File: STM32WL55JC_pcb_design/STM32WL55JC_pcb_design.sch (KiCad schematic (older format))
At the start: 32 parts, among them J1 Conn_01x03, J10 Conn_01x06_Male, J11 Conn_02x02_Odd_Even, J2 Conn_01x03, J3 Conn_02x05_Odd_Even, J4 Conn_01x03, J5 Conn_01x09, J6 Conn_01x09, J7 Conn_01x03, J8 Conn_01x09, J9 Conn_01x09, SW2 SW_MEC_5E, U1 STM32WL55JCI7, Y1 32MHz, Y2 32.768kHz

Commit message: Finish new design schematic
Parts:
- removed C13: 470nF, Capacitor_SMD:C_0805_2012Metric, symbol Device:C
- removed J10: Conn_01x06_Male, Connector_PinHeader_2.54mm:PinHeader_1x06_P2.54mm_Vertical, symbol Connector:Conn_01x06_Male
- removed J3: Conn_02x05_Odd_Even, Connector_PinHeader_1.27mm:PinHeader_2x05_P1.27mm_Vertical_SMD, symbol Connector_Generic:Conn_02x05_Odd_Even
- removed L1: 15uH, Inductor_SMD:L_0805_2012Metric, symbol pspice:INDUCTOR
- removed U1: STM32WL55JCI7, MCU_ST_STM3255JCI7:STM32WL55JCI7, symbol STM32WL55JC_pcb_design-rescue:STM32WL55JCI7-MCU_ST_STM3255JCI7
- added C11: 4.7F, Capacitor_SMD:C_0805_2012Metric, symbol Device:C
- added IC1: STM32F051R8T6, QFP50P1200X1200X160-64N, symbol STM32F051R8T6:STM32F051R8T6
- added J10: Conn_02x15_Odd_Even, symbol Connector_Generic:Conn_02x15_Odd_Even
- added J9: Conn_02x10_Odd_Even, symbol Connector_Generic:Conn_02x10_Odd_Even
- C12: renamed from C46; value 2.2pF -> 13pF
- C15: renamed from C53; value 2.2pF -> 13pF
- C3: value 100nF -> 4.7uF
- C6: renamed from C8; value 100nF -> 4.7uF
- C7: renamed from C9; value 100nF -> 10nF
- C8: renamed from C10; value 100nF -> 1uF
- Y1: footprint Oscillator:Oscillator_SMD_SeikoEpson_SG210-4Pin_2.5x2.0mm -> NX2016SA32MEXS00ACS06465:NX2016SA32MEXS00ACS06465
- renumbered C12 to C10, C47 to C13, C49 to C14, C7 to C5, C11 to C9, J4 to J3, J5 to J4, J6 to J5, J7 to J6, J8 to J7, J9 to J8, R7 to R1, SW2 to SW1
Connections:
- net labels added: ACC_ADC1, ACC_ADC2, ACC_ADC3, ACC_INT1, ACC_INT2, ADC_DIN, ADC_DOUT, ADC_SCLK, BOOT0, GPS_1PPS, GPS_AADET_N, GPS_EX_ANT, GPS_RESET, GPS_TIMER, LoRa_DO0, LoRa_DO1, LoRa_DO2, LoRa_DO3, LoRa_DO4, LoRa_DO5, LoRa_MISO, LoRa_MOSI, LoRa_NRST, LoRa_NSS, LoRa_RXTX_CTRL, LoRa_SCK, PA11, PB3, PB4, PC0, PC13, PD2, RTC_SQW, VDD
- net labels removed: ADC_DIN1, ADC_DIN2, ADC_DOUT1, ADC_DOUT2, ADC_SCLK1, ADC_SCLK2, PC5, RFI_N, RFI_P, RFO_HP, RFO_LP, RF_CTRL, SWO, VBAT, VDD1, VDD2, VDD3, VDD4, VDDA, VDDPA, VDDRF, VDDRF_1V55, VDDSMPS, VREF+, VR_PA
- wire segments 233 -> 160
- no-connect marks 10 -> 5
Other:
- moved on the sheet: C10, C12, C13, C14, C15, C5, C6, C7, C8, C9, J1, J11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

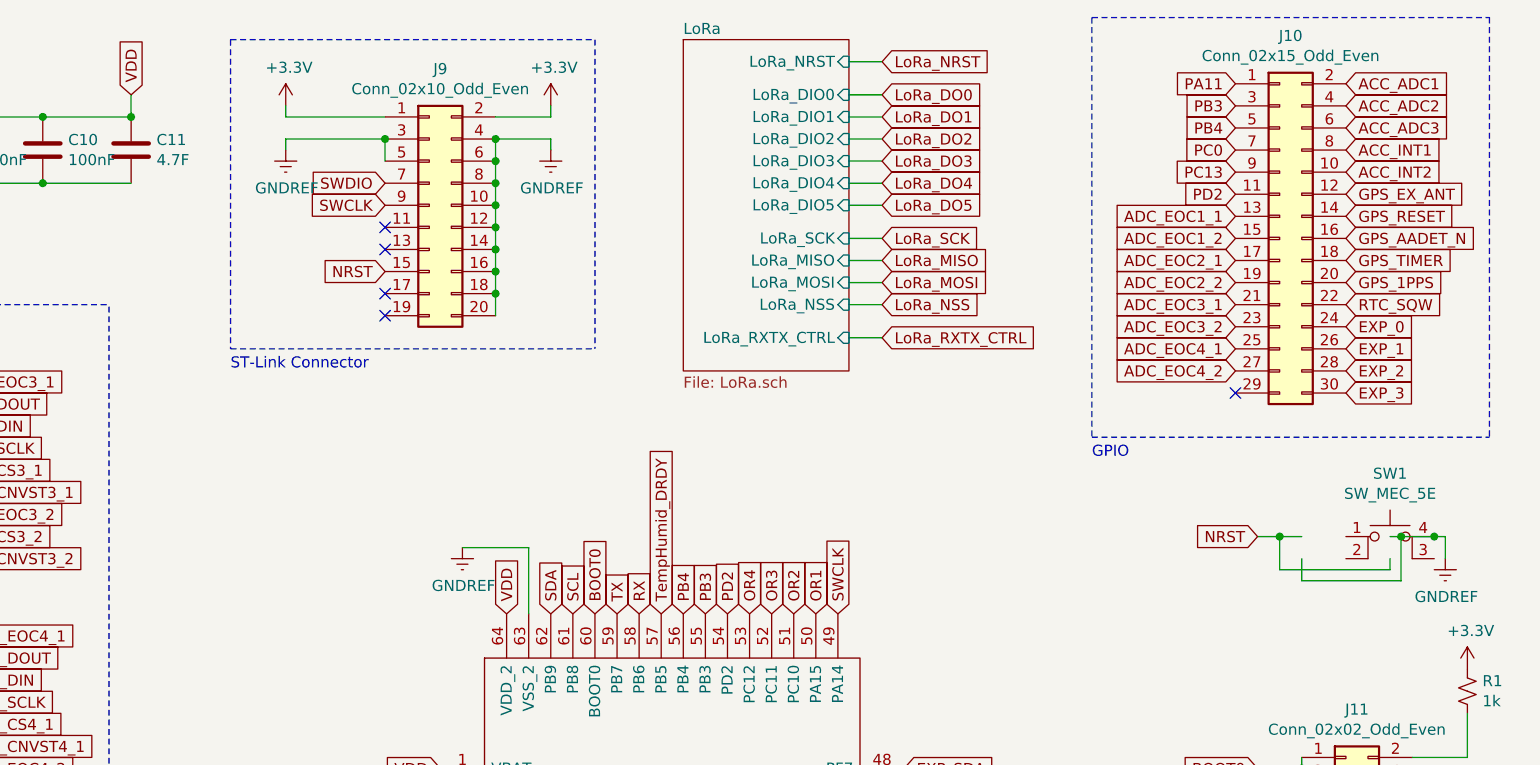
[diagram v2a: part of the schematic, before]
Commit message: Initial pcb layout and routing
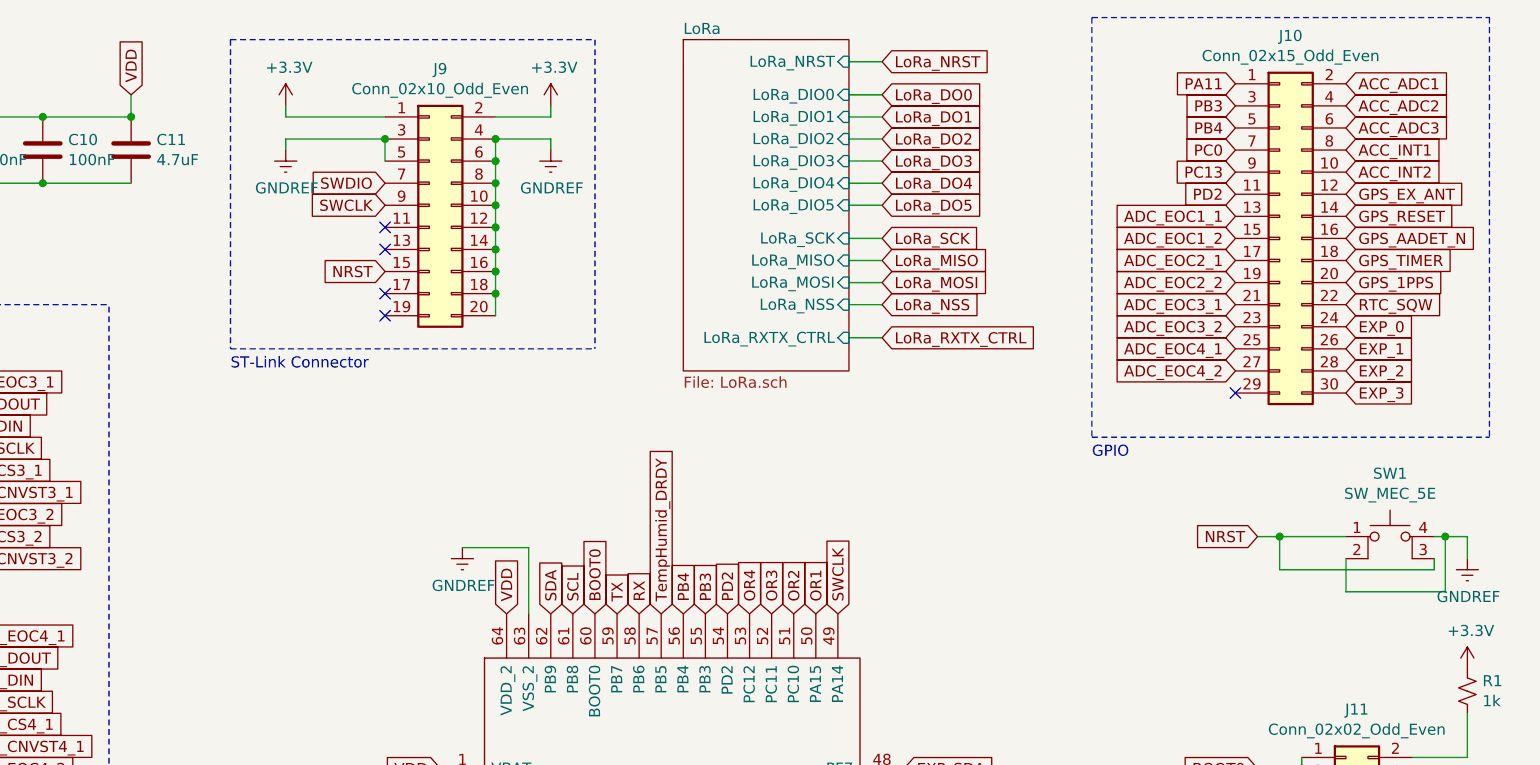
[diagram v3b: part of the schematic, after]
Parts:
- C11: value 4.7F -> 4.7uF
- C12, C15: footprint Capacitor_SMD:C_0805_2012Metric -> Capacitor_SMD:C_0402_1005Metric
- IC1: footprint QFP50P1200X1200X160-64N -> STM32F051R8T6:QFP50P1200X1200X160-64N
- J10: footprint (none) -> Connector_PinHeader_2.54mm:PinHeader_2x15_P2.54mm_Vertical
- J9: footprint (none) -> Connector_PinHeader_2.54mm:PinHeader_2x10_P2.54mm_Vertical
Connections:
- net GNDREF: now also SW1.2
- net NRST: now also SW1.1, SW1.3 (K)
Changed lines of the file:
@@
 F 0 "C12" H 9942 5246 50  0000 L CNN
 F 1 "13pF" H 9942 5155 50  0000 L CNN
-F 2 "Capacitor_SMD:C_0805_2012Metric" H 9850 5200 50  0001 C CNN
+F 2 "Capacitor_SMD:C_0402_1005Metric" H 9850 5200 50  0001 C CNN
 F 3 "~" H 9850 5200 50  0001 C CNN
 	1    9850 5200
@@
 F 0 "C15" H 10642 5246 50  0000 L CNN
 F 1 "13pF" H 10642 5155 50  0000 L CNN
-F 2 "Capacitor_SMD:C_0805_2012Metric" H 10550 5200 50  0001 C CNN
+F 2 "Capacitor_SMD:C_0402_1005Metric" H 10550 5200 50  0001 C CNN
 F 3 "~" H 10550 5200 50  0001 C CNN
 	1    10550 5200
@@
 $EndComp
 Wire Wire Line
-	10550 2900 10600 2900
-Wire Wire Line
-	10050 2900 10150 2900
-Wire Wire Line
-	10800 2900 10800 3000
+	10900 2900 10900 3000
 $Comp
 L power:GNDREF #PWR024
 U 1 1 6161C125
-P 10800 3000
-F 0 "#PWR024" H 10800 2750 50  0001 C CNN
-F 1 "GNDREF" H 10805 2827 50  0000 C CNN
-F 2 "" H 10800 3000 50  0001 C CNN
-F 3 "" H 10800 3000 50  0001 C CNN
-	1    10800 3000
+P 10900 3000
+F 0 "#PWR024" H 10900 2750 50  0001 C CNN
+F 1 "GNDREF" H 10905 2827 50  0000 C CNN
+F 2 "" H 10900 3000 50  0001 C CNN
+F 3 "" H 10900 3000 50  0001 C CNN
+	1    10900 3000
 	1    0    0    -1
 $EndComp
@@
 EXP_1
 Wire Wire Line
-	10150 3000 10150 3100
-Wire Wire Line
-	10150 3100 10600 3100
-Wire Wire Line
-	10600 3100 10600 2900
-Connection ~ 10600 2900
-Wire Wire Line
-	10600 2900 10750 2900
-Wire Wire Line
 	10050 2900 10050 3050
-Wire Wire Line
-	10050 3050 10550 3050
-Wire Wire Line
-	10550 3050 10550 3000
 Text GLabel 10350 1950 2    50   Input ~ 0
 EXP_0
@@
 F 0 "IC1" H 8394 3246 50  0000 L CNN
 F 1 "STM32F051R8T6" H 8394 3155 50  0000 L CNN
-F 2 "QFP50P1200X1200X160-64N" H 8200 4450 50  0001 L CNN
+F 2 "STM32F051R8T6:QFP50P1200X1200X160-64N" H 8200 4450 50  0001 L CNN
 F 3 "http://www.st.com/web/en/resource/technical/document/datasheet/DM00039193.pdf" H 8200 4350 50  0001 L CNN
 F 4 "STMICROELECTRONICS - STM32F051R8T6 - ARM MCU, Access Line, STM32 Family STM32F0 Series Microcontrollers, ARM Cortex-M0, 32bit, 48 MHz" H 8200 4250 50  0001 L CNN "Description"
@@
 F 0 "J9" H 6250 2017 50  0000 C CNN
 F 1 "Conn_02x10_Odd_Even" H 6250 1926 50  0000 C CNN
-F 2 "" H 6200 1400 50  0001 C CNN
+F 2 "Connector_PinHeader_2.54mm:PinHeader_2x10_P2.54mm_Vertical" H 6200 1400 50  0001 C CNN
 F 3 "~" H 6200 1400 50  0001 C CNN
 	1    6200 1400
@@
 AR Path="/61D7468A" Ref="C11"  Part="1"
 F 0 "C11" H 4965 1196 50  0000 L CNN
-F 1 "4.7F" H 4965 1105 50  0000 L CNN
+F 1 "4.7uF" H 4965 1105 50  0000 L CNN
 F 2 "Capacitor_SMD:C_0805_2012Metric" H 4888 1000 50  0001 C CNN
 F 3 "~" H 4850 1150 50  0001 C CNN
@@
 	1    0    0    -1
 $EndComp
-Connection ~ 10750 2900
-Wire Wire Line
-	10750 2900 10800 2900
 Wire Wire Line
 	4450 1000 4850 1000
@@
 F 0 "J10" H 10100 2467 50  0000 C CNN
 F 1 "Conn_02x15_Odd_Even" H 10100 2376 50  0000 C CNN
-F 2 "" H 10050 1550 50  0001 C CNN
+F 2 "Connector_PinHeader_2.54mm:PinHeader_2x15_P2.54mm_Vertical" H 10050 1550 50  0001 C CNN
 F 3 "~" H 10050 1550 50  0001 C CNN
 	1    10050 1550
@@
 Wire Notes Line
 	9200 550  9200 2450
+Wire Wire Line
+	10050 2900 10350 2900
+Wire Wire Line
+	10750 3050 10750 3000
+Wire Wire Line
+	10050 3050 10750 3050
+Wire Wire Line
+	10750 2900 10800 2900
+Wire Wire Line
+	10350 3000 10350 3150
+Wire Wire Line
+	10350 3150 10800 3150
+Wire Wire Line
+	10800 3150 10800 2900
+Connection ~ 10800 2900
+Wire Wire Line
+	10800 2900 10900 2900
 $EndSCHEMATC

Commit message: Finish pcb routing
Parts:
- removed J10: Conn_02x15_Odd_Even, Connector_PinHeader_2.54mm:PinHeader_2x15_P2.54mm_Vertical, symbol Connector_Generic:Conn_02x15_Odd_Even
- added J10: Conn_01x08_Male, Connector_PinHeader_2.54mm:PinHeader_1x08_P2.54mm_Vertical, symbol Connector:Conn_01x08_Male
- added J22: Conn_01x20_Male, Connector_PinHeader_2.54mm:PinHeader_1x20_P2.54mm_Vertical, symbol Connector:Conn_01x20_Male
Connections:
- net ACC_ADC1: now also J22.7 (Pin_7)
- net ACC_ADC2: now also J22.8 (Pin_8)
- net ACC_ADC3: now also J22.9 (Pin_9)
- net ACC_INT1: now also J22.10 (Pin_10)
- net ACC_INT2: now also J22.11 (Pin_11)
- net ADC_CNVST1_1: now also IC1.11 (PC3); no longer IC1.9 (PC1)
- net ADC_CNVST1_2: now also IC1.9 (PC1); no longer IC1.10 (PC2)
- net ADC_CNVST2_1: now also IC1.17 (PA3); no longer IC1.11 (PC3)
- net ADC_CNVST2_2: now also IC1.15 (PA1); no longer IC1.14 (PA0)
- net ADC_CNVST3_1: now also IC1.24 (PC4); no longer IC1.15 (PA1)
- net ADC_CNVST3_2: now also IC1.19 (PF5); no longer IC1.16 (PA2)
- net ADC_CNVST4_2: now also IC1.26 (PB0); no longer IC1.29 (PB10)
- net ADC_CS1_1: now also IC1.14 (PA0); no longer IC1.17 (PA3)
- net ADC_CS1_2: now also IC1.10 (PC2); no longer IC1.18 (PF4)
- net ADC_CS2_1: now also IC1.18 (PF4); no longer IC1.19 (PF5)
- net ADC_CS2_2: now also IC1.16 (PA2); no longer IC1.20 (PA4)
- net ADC_CS3_1: now also IC1.25 (PC5); no longer IC1.24 (PC4)
- net ADC_CS3_2: now also IC1.20 (PA4); no longer IC1.25 (PC5)
- net ADC_CS4_1: now also IC1.29 (PB10); no longer IC1.26 (PB0)
- net ADC_EOC1_1: now also J10.7 (Pin_7)
- net ADC_EOC1_2: now also J10.8 (Pin_8)
- net ADC_EOC2_1: now also J10.5 (Pin_5)
- net ADC_EOC2_2: now also J10.6 (Pin_6)
- net ADC_EOC3_1: now also J10.3 (Pin_3)
- net ADC_EOC3_2: now also J10.4 (Pin_4)
- net ADC_EOC4_1: now also J10.1 (Pin_1)
- net ADC_EOC4_2: now also J10.2 (Pin_2)
- net EXP_0: now also J22.20 (Pin_20)
- net EXP_1: now also J22.19 (Pin_19)
- net EXP_2: now also J22.18 (Pin_18)
- net EXP_3: now also J22.17 (Pin_17)
- net GNDREF: now also J9.13 (Pin_13)
- net GPS_1PPS: now also J22.16 (Pin_16)
- net GPS_AADET_N: now also J22.14 (Pin_14)
- net GPS_EX_ANT: now also J22.12 (Pin_12)
- net GPS_RESET: now also J22.13 (Pin_13)
- net GPS_TIMER: now also J22.15 (Pin_15)
- net OR1: now also IC1.53 (PC12); no longer IC1.50 (PA15)
- net OR2: now also IC1.52 (PC11); no longer IC1.51 (PC10)
- net OR3: now also IC1.50 (PA15); no longer IC1.52 (PC11)
- net OR4: now also IC1.51 (PC10); no longer IC1.53 (PC12)
- net PA11: now also J22.6 (Pin_6)
- net PB3: now also J22.4 (Pin_4)
- net PB4: now also J22.3 (Pin_3)
- net PC0: now also J22.1 (Pin_1)
- net PC13: now also J22.2 (Pin_2)
- net PD2: now also J22.5 (Pin_5)
- no-connect marks 5 -> 3
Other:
- moved on the sheet: C12, C13, C14, C15, J11, R1, SW1, Y1, Y2

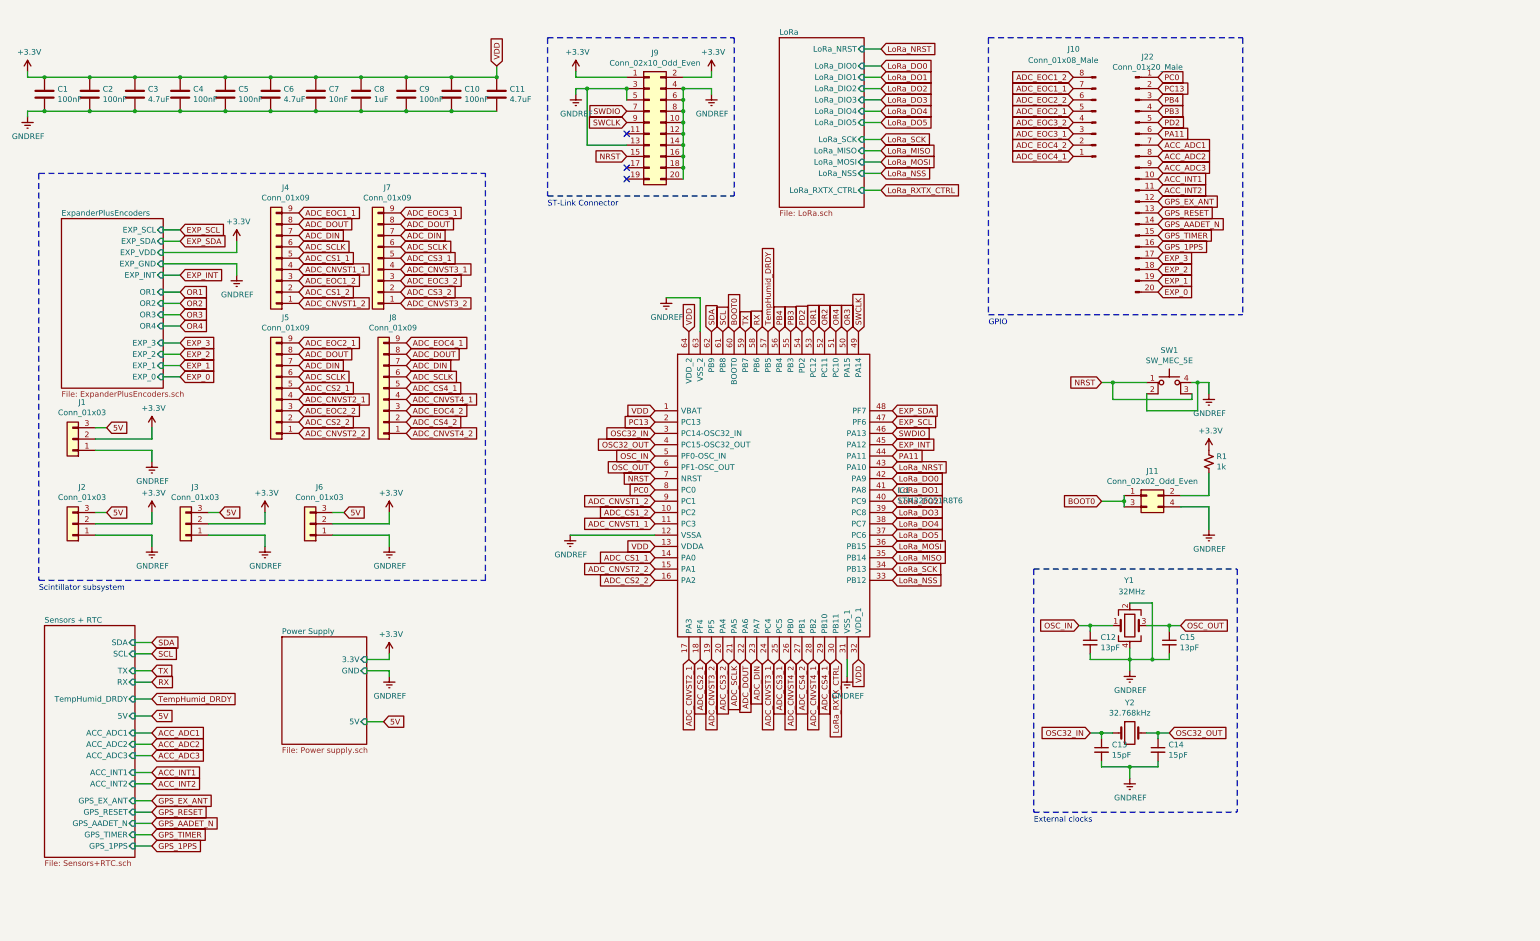
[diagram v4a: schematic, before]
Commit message: Change devices to available ones from JLC
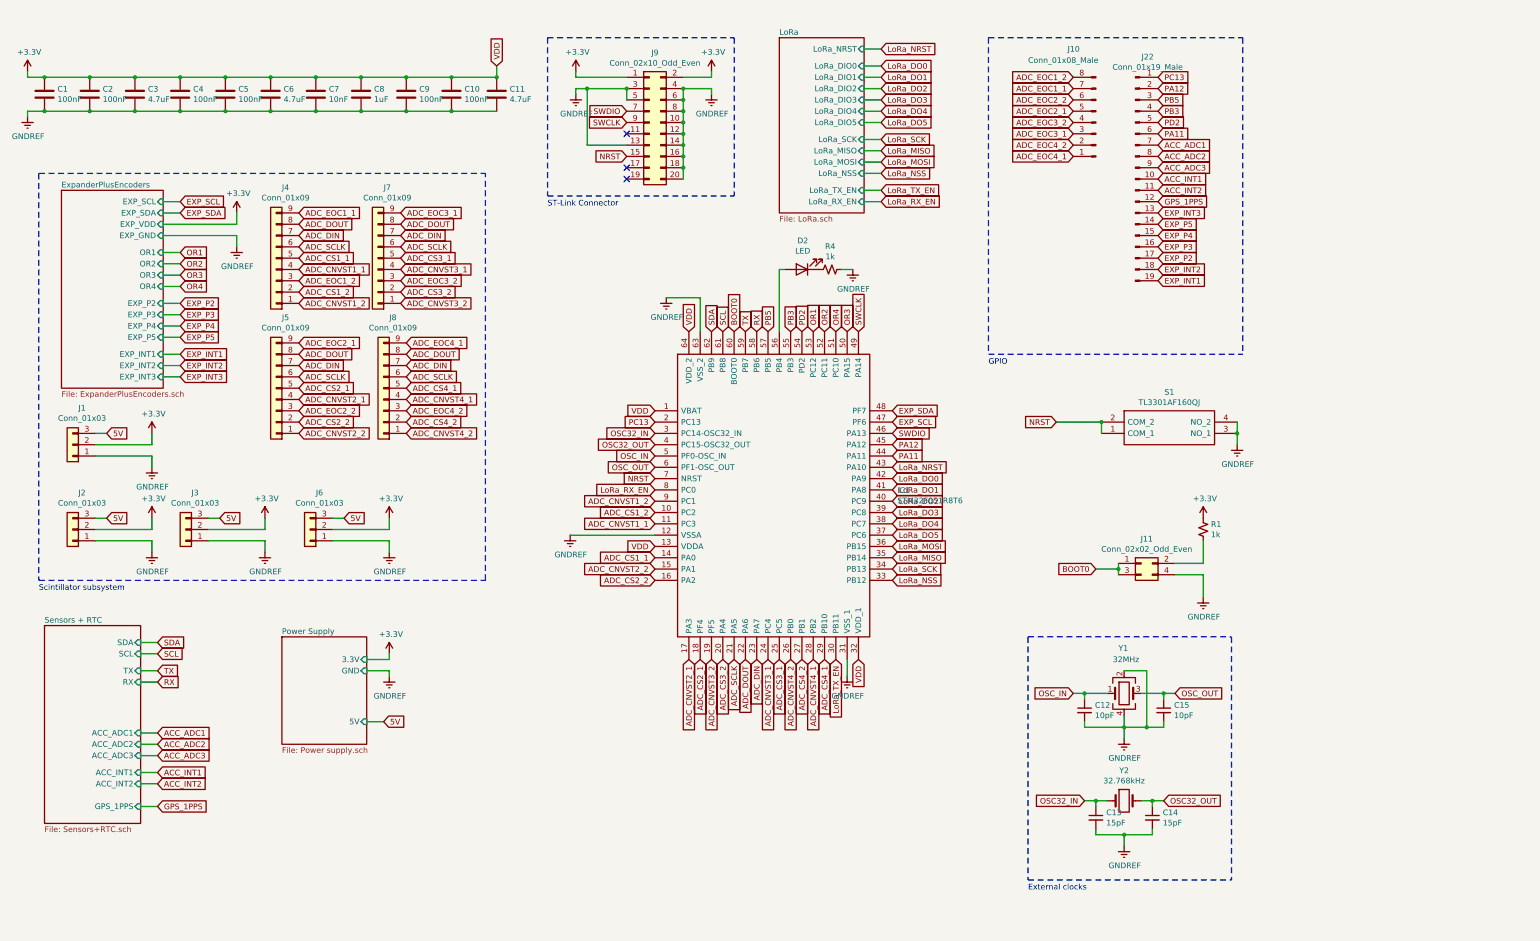
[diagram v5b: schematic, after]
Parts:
- removed J22: Conn_01x20_Male, Connector_PinHeader_2.54mm:PinHeader_1x20_P2.54mm_Vertical, symbol Connector:Conn_01x20_Male
- removed SW1: SW_MEC_5E, EVQ-P2F02K:EVQP2V02W, symbol Switch:SW_MEC_5E
- added D2: LED, LED_SMD:LED_0805_2012Metric, symbol Device:LED
- added J22: Conn_01x19_Male, Connector_PinHeader_2.54mm:PinHeader_1x19_P2.54mm_Vertical, symbol Connector:Conn_01x19_Male
- added R4: 1k, Resistor_SMD:R_0805_2012Metric, symbol Device:R_Small_US
- added S1: TL3301AF160QJ, TL3301AF160QJ:TL3301AF160QJ, symbol TL3301AF160QJ:TL3301AF160QJ
- C12, C15: value 13pF -> 10pF; footprint Capacitor_SMD:C_0402_1005Metric -> Capacitor_SMD:C_0805_2012Metric
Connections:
- net ACC_ADC1: now also J22.7 (Pin_7)
- net ACC_ADC2: now also J22.8 (Pin_8)
- net ACC_ADC3: now also J22.9 (Pin_9)
- net ACC_INT1: now also J22.10 (Pin_10)
- net ACC_INT2: now also J22.11 (Pin_11)
- net GNDREF: now also R4.1, S1.3 (NO_1), S1.4 (NO_2)
- net GPS_1PPS: now also J22.12 (Pin_12)
- net NRST: now also S1.1 (COM_1), S1.2 (COM_2)
- net PA11: now also J22.6 (Pin_6)
- net PB3: now also J22.4 (Pin_4)
- net PC13: now also J22.1 (Pin_1)
- net PD2: now also J22.5 (Pin_5)
- net EXP_INT renamed PA12
- net PA12: now also J22.2 (Pin_2)
- net LoRa_RXTX_CTRL renamed LoRa_TX_EN
- net PB4: no longer names the net of IC1.56 (PB4)
- net PB4: now also D2.2 (A)
- net PC0 renamed LoRa_RX_EN
- net TempHumid_DRDY renamed PB5
- net PB5: now also J22.3 (Pin_3)
- new net: D2.1 (K), R4.2
- new net EXP_INT1: J22.19 (Pin_19)
- new net EXP_INT2: J22.18 (Pin_18)
- new net EXP_INT3: J22.13 (Pin_13)
- new net EXP_P2: J22.17 (Pin_17)
- new net EXP_P3: J22.16 (Pin_16)
- new net EXP_P4: J22.15 (Pin_15)
- new net EXP_P5: J22.14 (Pin_14)
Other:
- moved on the sheet: C12, C13, C14, C15, J1, J11, J2, J3, J6, R1, Y1, Y2

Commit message: Finish silk screen
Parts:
- added TP1: Micro_VDD, TestPoint:TestPoint_Pad_D4.0mm, symbol Connector:TestPoint
- added TP2: Micro_GND, TestPoint:TestPoint_Pad_D4.0mm, symbol Connector:TestPoint
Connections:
- net +3V3: now also TP1.1
- net GNDREF: now also TP2.1
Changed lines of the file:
@@
 Text GLabel 10700 2300 2    50   Input ~ 0
 EXP_P5
+Text GLabel 6900 7700 3    50   Input ~ 0
+VDD
+$Comp
+L power:GNDREF #PWR0101
+U 1 1 61855E4F
+P 7400 7700
+F 0 "#PWR0101" H 7400 7450 50  0001 C CNN
+F 1 "GNDREF" H 7405 7527 50  0000 C CNN
+F 2 "" H 7400 7700 50  0001 C CNN
+F 3 "" H 7400 7700 50  0001 C CNN
+	1    7400 7700
+	1    0    0    -1
+$EndComp
+$Comp
+L Connector:TestPoint TP1
+U 1 1 618577EB
+P 6900 7700
+F 0 "TP1" H 6958 7818 50  0000 L CNN
+F 1 "Micro_VDD" H 6958 7727 50  0000 L CNN
+F 2 "TestPoint:TestPoint_Pad_D4.0mm" H 7100 7700 50  0001 C CNN
+F 3 "~" H 7100 7700 50  0001 C CNN
+	1    6900 7700
+	1    0    0    -1
+$EndComp
+$Comp
+L Connector:TestPoint TP2
+U 1 1 61858267
+P 7400 7700
+F 0 "TP2" H 7458 7818 50  0000 L CNN
+F 1 "Micro_GND" H 7458 7727 50  0000 L CNN
+F 2 "TestPoint:TestPoint_Pad_D4.0mm" H 7600 7700 50  0001 C CNN
+F 3 "~" H 7600 7700 50  0001 C CNN
+	1    7400 7700
+	1    0    0    -1
+$EndComp
 $EndSCHEMATC
